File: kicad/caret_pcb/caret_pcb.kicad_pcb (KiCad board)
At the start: 2 copper layers, 56.2 x 160.2 mm, 49 parts, among them J1 RAMPS POWER IN, J10 SIGNAL IN, J11 Endstop Y, J12 X+, J13 Y+, J14 Raspberry_Pi_2_3, J15 PWR IN, J2 RAMPS IN, J3 FC PWR OUT, J4 FC SIGNAL OUT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

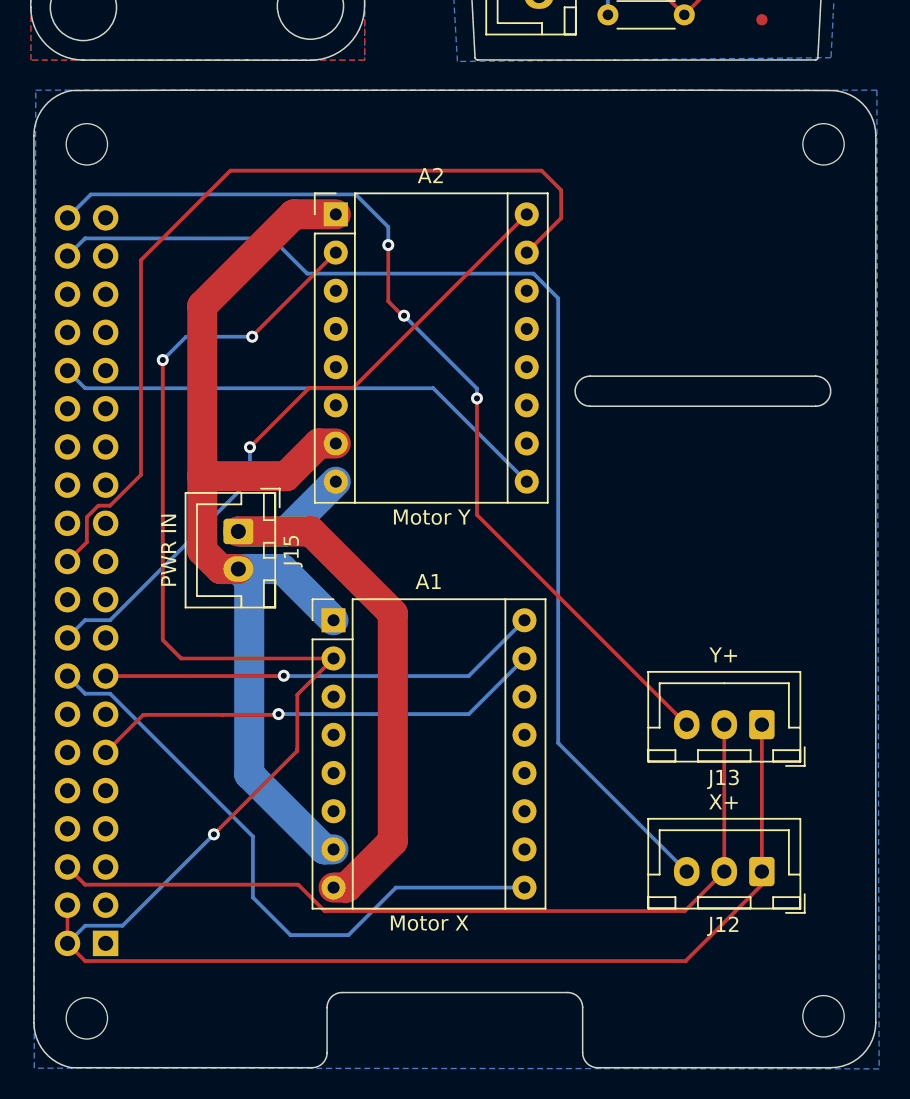
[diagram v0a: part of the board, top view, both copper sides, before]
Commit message: caret_pcb: fix power line
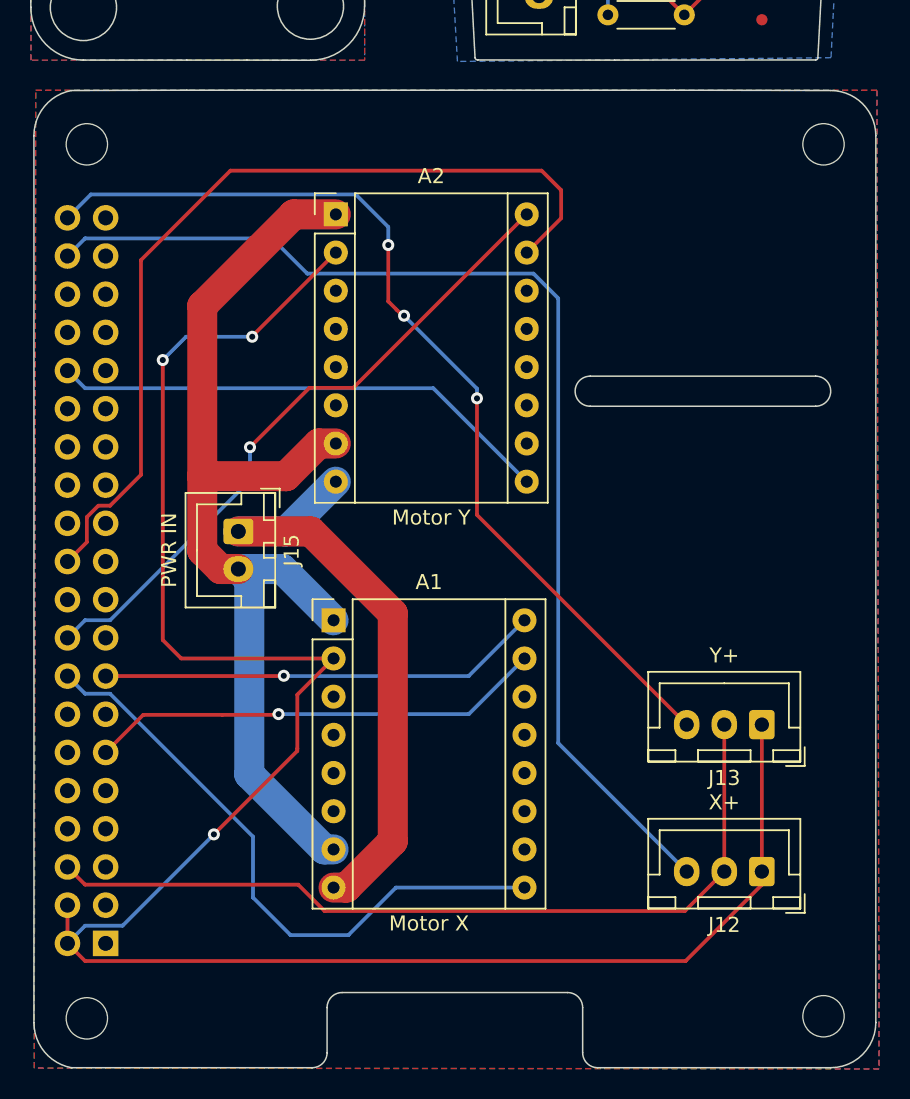
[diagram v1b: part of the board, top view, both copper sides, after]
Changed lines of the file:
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@@
+    )
+  )
+  (zone (net 1) (net_name "/RAMPS Adapter/HE0+") (layer "F.Cu") (hatch edge 0.508)
+    (connect_pads (clearance 1.25))
+    (min_thickness 0.254) (filled_areas_thickness no)
+    (fill yes (thermal_gap 0.508) (thermal_bridge_width 0.508))
+    (polygon
+      (pts
+        (xy 76.8 184.8125)
+        (xy 20.6 184.7625)
+        (xy 20.7 119.7125)
+        (xy 76.65 119.7125)
+      )
     )
   )

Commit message: caret_pcb: fix piezo sensor power line, fix rpi shield schematic
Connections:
- J12 pad 1: Net-(A1-Pad2) -> Net-(J12-Pad1)
- J13 pad 1: Net-(A1-Pad2) -> Net-(J12-Pad1)
- J14 pad 17: unconnected-(J14-Pad17) -> Net-(J12-Pad1)
- J14 pad 2: Net-(A1-Pad2) -> unconnected-(J14-Pad2)
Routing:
- net Net-(J12-Pad1): track 0.00 -> 76.9 mm, vias 0 -> 1
- net Net-(A1-Pad2): track 134.7 -> 72.7 mm
- removed copper zone on B.Cu, net /RPi Motor/GNDmot
